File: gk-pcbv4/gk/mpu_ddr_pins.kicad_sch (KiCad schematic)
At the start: 1 part, among them U5 STM32MP255DAI3

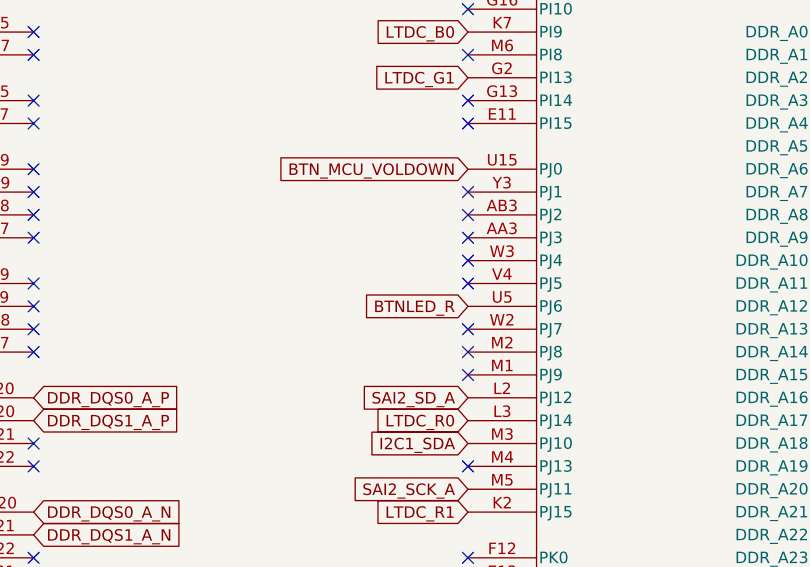
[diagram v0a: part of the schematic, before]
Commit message: Add UART6 out for debug
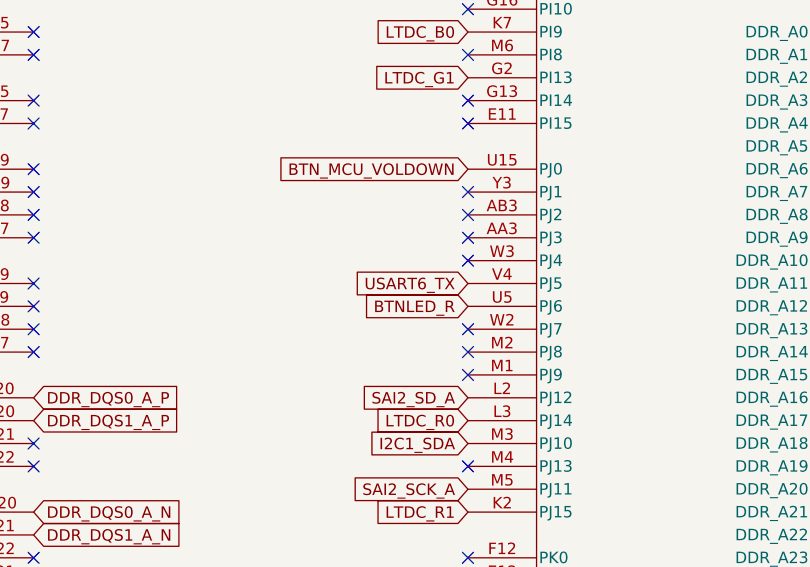
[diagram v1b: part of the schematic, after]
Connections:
- net USART6_TX: now reaches U5.V4 (PJ5)
- no-connect marks 89 -> 88
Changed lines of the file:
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@@
-	)
-	(no_connect
-		(at 162.56 92.71)
 	)
 	(no_connect
@@
 			(effects
 				(font
+					(size 1.27 1.27)
+				)
+				(justify right)
+				(hide yes)
+			)
+		)
+	)
+	(global_label "USART6_TX"
+		(shape input)
+		(at 162.56 92.71 180)
+		(fields_autoplaced yes)
+		(effects
+			(font
+				(size 1.27 1.27)
+			)
+			(justify right)
+		)
+		(property "Intersheetrefs" "${INTERSHEET_REFS}"
+			(at 149.3544 92.71 0)
+			(effects
+				(font

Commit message: pcb order 20251115
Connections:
- net BOOT1 is gone; now on net GND: U5.R3 (BOOT1)
- net BOOT0 renamed GND
- net BOOT2 renamed VDDIO

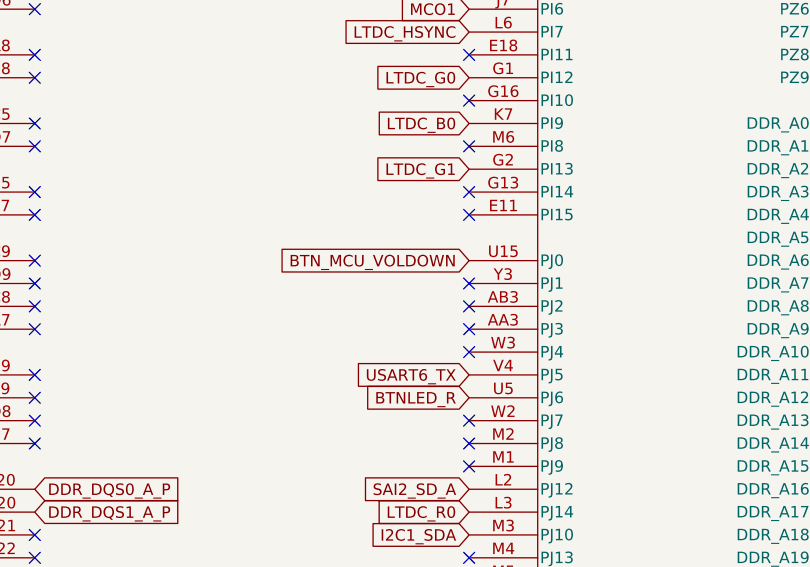
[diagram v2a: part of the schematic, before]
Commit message: add usart6 connection to schematic
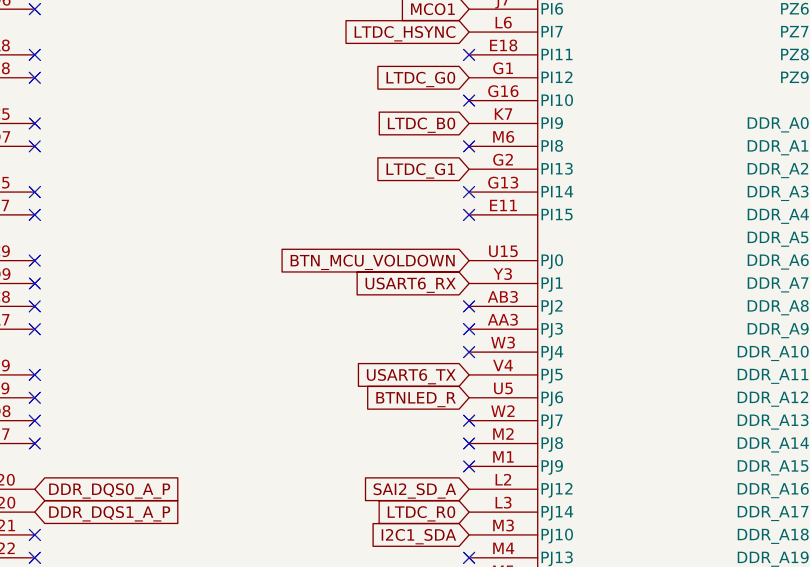
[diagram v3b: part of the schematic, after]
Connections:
- net USART6_RX: now reaches U5.Y3 (PJ1)
- no-connect marks 88 -> 87
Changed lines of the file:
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@@
-	)
-	(no_connect
-		(at 162.56 82.55)
 	)
 	(no_connect
@@
 				(hide yes)
 			)
+		)
+	)
+	(global_label "USART6_RX"
+		(shape input)
+		(at 162.56 82.55 180)
+		(fields_autoplaced yes)
+		(effects
+			(font
+				(size 1.27 1.27)
+			)
+			(justify right)
+		)
+		(property "Intersheetrefs" "${INTERSHEET_REFS}"
+			(at 149.052 82.55 0)
+			(effects
+				(font
+					(size 1.27 1.27)
+				)
+				(justify right)
+				(hide yes)
+			)
